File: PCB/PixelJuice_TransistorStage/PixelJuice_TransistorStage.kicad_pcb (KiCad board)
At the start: 2 copper layers, 33.2 x 35.3 mm, 12 parts, among them J1 INPUT_PORT, J2 OUTPUT_PORT, Q1 2N3904, Q2 2N3904, Q3 2N3904

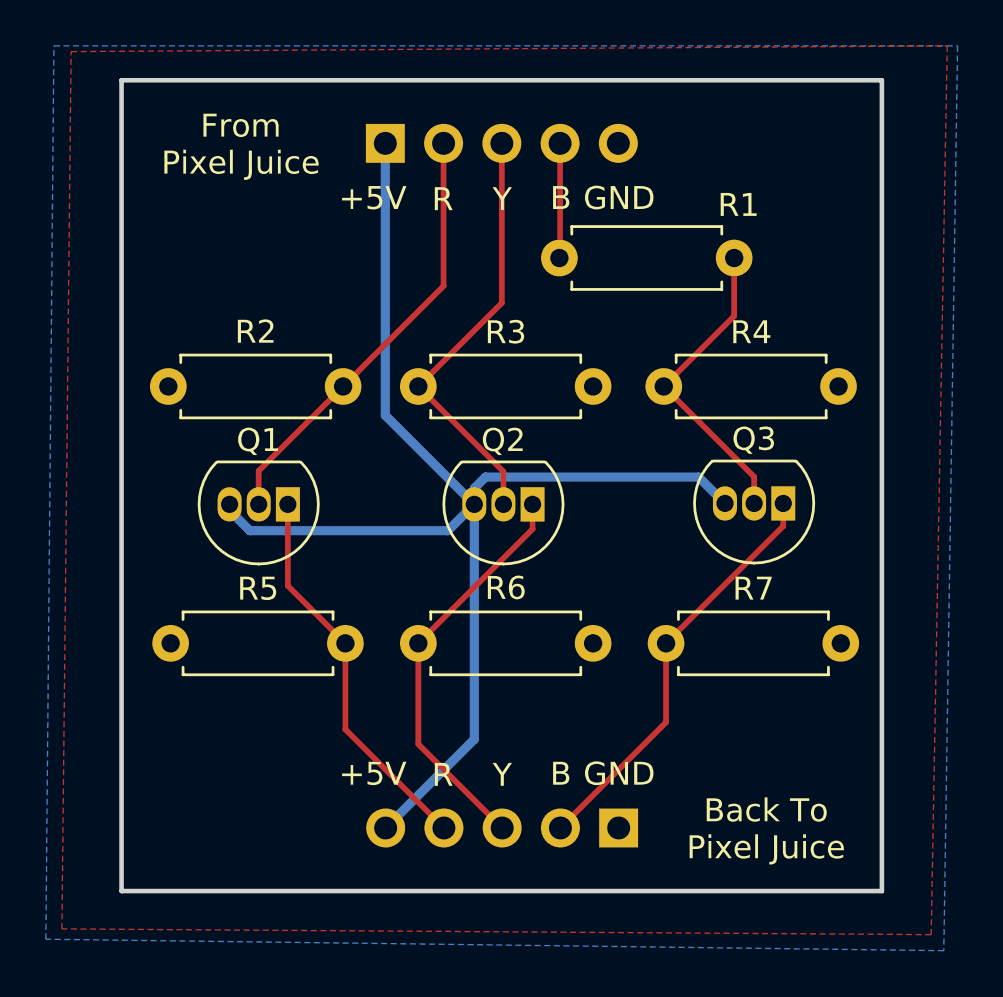
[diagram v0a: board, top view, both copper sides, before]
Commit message: added 2 new soundcard designs
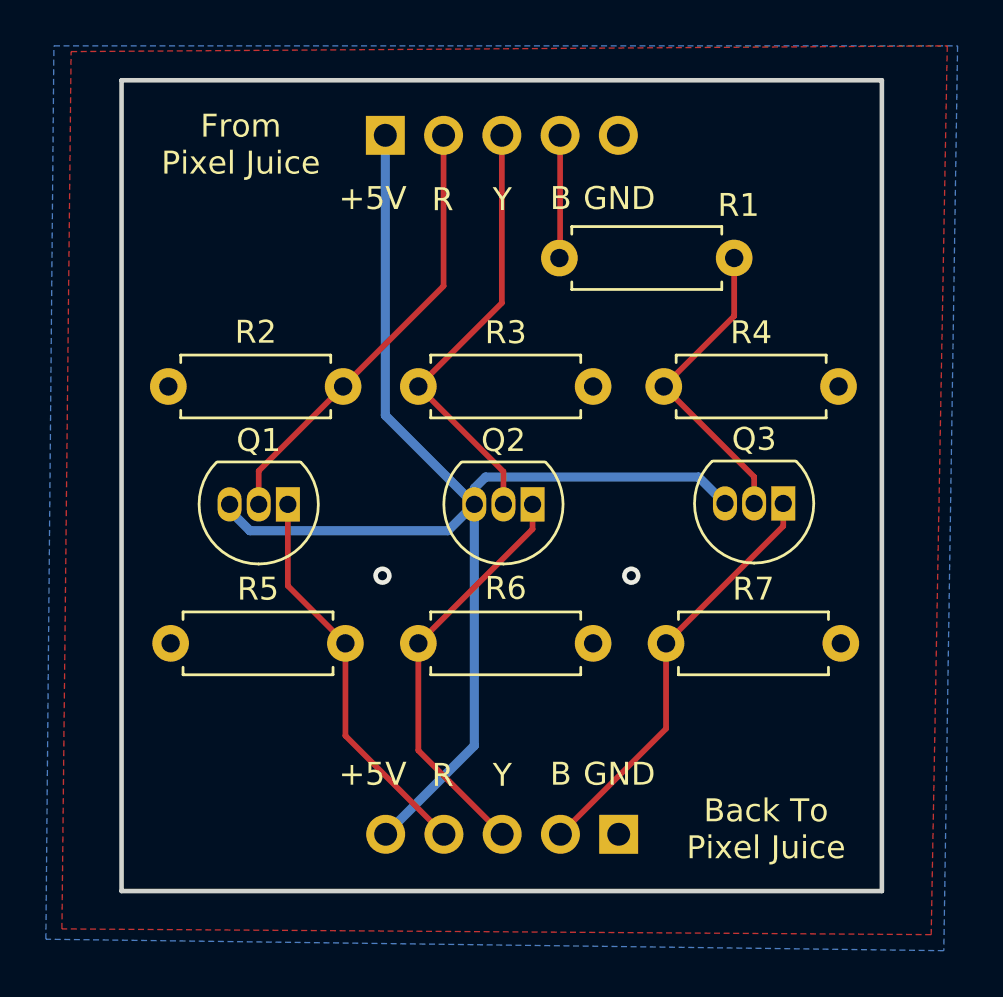
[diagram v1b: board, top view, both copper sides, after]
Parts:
- moved J1 0.35 mm to (142.2, 73.8)
- moved J2 0.28 mm to (152.3, 104.3)
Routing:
- net +5V: track 57.1 -> 57.8 mm
- net GND: vias 0 -> 2
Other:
- board text added: "JLCJLCJLCJLC"
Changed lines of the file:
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@@
       (outputformat 1)
       (mirror false)
-      (drillshape 1)
+      (drillshape 0)
       (scaleselection 1)
-      (outputdirectory "")
+      (outputdirectory "gerbers/")
     )
   )
@@
   )
   (footprint "Connector_PinHeader_2.54mm:PinHeader_1x05_P2.54mm_Vertical" (layer "B.Cu")
-    (at 152.325 104.05 90)
+    (at 152.325 104.325 90)
     (descr "Through hole straight pin header, 1x05, 2.54mm pitch, single row")
     (tags "Through hole pin header THT 1x05 2.54mm single row")
@@
     (property "Sheetname" "")
     (attr through_hole)
-    (fp_text reference "J2" (at 0 2.33 90) (layer "B.SilkS")
+    (fp_text reference "J2" (at 0 -12.575 90) (layer "B.SilkS")
       (effects (font (size 1 1) (thickness 0.15)) (justify mirror))
     )
@@
   )
   (footprint "Connector_PinHeader_2.54mm:PinHeader_1x05_P2.54mm_Vertical" (layer "B.Cu")
-    (at 142.15 74.2 -90)
+    (at 142.15 73.85 -90)
     (descr "Through hole straight pin header, 1x05, 2.54mm pitch, single row")
     (tags "Through hole pin header THT 1x05 2.54mm single row")
@@
   )
   (gr_rect (start 130.65 71.45) (end 163.8 106.8) (layer "Edge.Cuts") (width 0.2) (fill none))
+  (gr_text "JLCJLCJLCJLC" (at 147.325 99.725) (layer "B.SilkS")
+    (effects (font (size 1 1) (thickness 0.2)) (justify mirror))
+  )
   (gr_text "Transistor Stage v1\nfor Pixel Juice\nNate Rivard, 2023" (at 147 79.25) (layer "B.SilkS")
     (effects (font (size 1 1) (thickness 0.15)) (justify left mirror))
@@
   )
   (dimension (type aligned) (layer "Cmts.User")
-    (pts (xy 152.325 104.05) (xy 152.325 74.2))
-    (height 15.8)
-    (gr_text "29.8500 mm" (at 166.975 89.125 90) (layer "Cmts.User")
-      (effects (font (size 1 1) (thickness 0.15)))
-    )
-    (format (units 3) (units_format 1) (precision 4))
-    (style (thickness 0.15) (arrow_length 1.27) (text_position_mode 0) (extension_height 0.58642) (extension_offset 0.5) keep_text_aligned)
-  )
-  (dimension (type aligned) (layer "Cmts.User")
     (pts (xy 132.7 71.45) (xy 132.7 106.8))
     (height 6.449999)
@@
   )
   (dimension (type aligned) (layer "Cmts.User")
-    (pts (xy 142.125 74.2) (xy 142.125 71.45))
+    (pts (xy 142.15 73.85) (xy 142.15 71.45))
     (height -5.025)
-    (gr_text "2.7500 mm" (at 135.95 72.825 90) (layer "Cmts.User")
-      (effects (font (size 1 1) (thickness 0.15)))
-    )
-    (format (units 3) (units_format 1) (precision 4))
-    (style (thickness 0.15) (arrow_length 1.27) (text_position_mode 0) (extension_height 0.58642) (extension_offset 0.5) keep_text_aligned)
-  )
-  (dimension (type aligned) (layer "Cmts.User")
-    (pts (xy 152.325 104.05) (xy 152.325 106.8))
-    (height -5.625)
-    (gr_text "2.7500 mm" (at 156.8 105.425 90) (layer "Cmts.User")
+    (gr_text "2.4000 mm" (at 135.975 72.65 90) (layer "Cmts.User")
       (effects (font (size 1 1) (thickness 0.15)))
     )
@@
     (style (thickness 0.15) (arrow_length 1.27) (text_position_mode 0) (extension_height 0.58642) (extension_offset 0.5) keep_text_aligned)
   )
-  (segment (start 146.03 100.185) (end 142.165 104.05) (width 0.4) (layer "B.Cu") (net 1))
+  (dimension (type aligned) (layer "Cmts.User")
+    (pts (xy 152.325 104.325) (xy 152.325 106.8))
+    (height -16.525)
+    (gr_text "2.4750 mm" (at 167.7 105.5625 90) (layer "Cmts.User")
+      (effects (font (size 1 1) (thickness 0.15)))
+    )
+    (format (units 3) (units_format 1) (precision 4))
+    (style (thickness 0.15) (arrow_length 1.27) (text_position_mode 0) (extension_height 0.58642) (extension_offset 0.5) keep_text_aligned)
+  )
+  (dimension (type aligned) (layer "Cmts.User")
+    (pts (xy 152.25 104.325) (xy 152.275 73.85))
+    (height 20.954074)
+    (gr_text "30.4750 mm" (at 172.066567 89.103747 89.95299773) (layer "Cmts.User")
+      (effects (font (size 1 1) (thickness 0.15)))
+    )
+    (format (units 3) (units_format 1) (precision 4))
+    (style (thickness 0.15) (arrow_length 1.27) (text_position_mode 0) (extension_height 0.58642) (extension_offset 0.5) keep_text_aligned)
+  )
+  (segment (start 142.15 73.85) (end 142.15 86.06) (width 0.4) (layer "B.Cu") (net 1))
   (segment (start 136.247052 91.08952) (end 135.36 90.202468) (width 0.4) (layer "B.Cu") (net 1))
   (segment (start 146.03 89.24) (end 146.52 88.75) (width 0.4) (layer "B.Cu") (net 1))
-  (segment (start 142.15 86.06) (end 146.03 89.94) (width 0.4) (layer "B.Cu") (net 1))
   (segment (start 135.36 90.202468) (end 135.36 89.94) (width 0.4) (layer "B.Cu") (net 1))
   (segment (start 155.81 88.75) (end 156.96 89.9) (width 0.4) (layer "B.Cu") (net 1))
-  (segment (start 146.03 89.94) (end 146.03 100.185) (width 0.4) (layer "B.Cu") (net 1))
-  (segment (start 142.15 74.2) (end 142.15 86.06) (width 0.4) (layer "B.Cu") (net 1))
+  (segment (start 142.15 86.06) (end 146.03 89.94) (width 0.4) (layer "B.Cu") (net 1))
   (segment (start 144.88048 91.08952) (end 136.247052 91.08952) (width 0.4) (layer "B.Cu") (net 1))
   (segment (start 146.52 88.75) (end 155.81 88.75) (width 0.4) (layer "B.Cu") (net 1))
+  (segment (start 146.03 89.94) (end 146.03 100.46) (width 0.4) (layer "B.Cu") (net 1))
+  (segment (start 146.03 100.46) (end 142.165 104.325) (width 0.4) (layer "B.Cu") (net 1))
   (segment (start 146.03 89.94) (end 146.03 89.24) (width 0.4) (layer "B.Cu") (net 1))
   (segment (start 146.03 89.94) (end 144.88048 91.08952) (width 0.4) (layer "B.Cu") (net 1))
   (segment (start 140.31 84.8) (end 136.63 88.48) (width 0.25) (layer "F.Cu") (net 2))
+  (segment (start 136.63 88.48) (end 136.63 89.94) (width 0.25) (layer "F.Cu") (net 2))
+  (segment (start 144.69 73.85) (end 144.69 80.42) (width 0.25) (layer "F.Cu") (net 2))
   (segment (start 144.69 80.42) (end 140.31 84.8) (width 0.25) (layer "F.Cu") (net 2))
-  (segment (start 136.63 88.48) (end 136.63 89.94) (width 0.25) (layer "F.Cu") (net 2))
-  (segment (start 144.69 74.2) (end 144.69 80.42) (width 0.25) (layer "F.Cu") (net 2))
-  (segment (start 147.23 74.2) (end 147.23 81.16) (width 0.25) (layer "F.Cu") (net 3))
+  (segment (start 147.23 73.85) (end 147.23 81.16) (width 0.25) (layer "F.Cu") (net 3))
   (segment (start 143.59 84.8) (end 147.3 88.51) (width 0.25) (layer "F.Cu") (net 3))
   (segment (start 147.3 88.51) (end 147.3 89.94) (width 0.25) (layer "F.Cu") (net 3))
   (segment (start 147.23 81.16) (end 143.59 84.8) (width 0.25) (layer "F.Cu") (net 3))
+  (segment (start 149.77 73.85) (end 149.77 79.17) (width 0.25) (layer "F.Cu") (net 4))
   (segment (start 149.77 79.17) (end 149.74 79.2) (width 0.25) (layer "F.Cu") (net 4))
-  (segment (start 149.77 74.2) (end 149.77 79.17) (width 0.25) (layer "F.Cu") (net 4))
+  (via (at 152.875 93.05) (size 0.8) (drill 0.4) (layers "F.Cu" "B.Cu") (free) (net 5))
+  (via (at 142.025 93.05) (size 0.8) (drill 0.4) (layers "F.Cu" "B.Cu") (free) (net 5))
   (segment (start 137.9 93.49) (end 140.41 96) (width 0.25) (layer "F.Cu") (net 6))
   (segment (start 137.9 89.94) (end 137.9 93.49) (width 0.25) (layer "F.Cu") (net 6))
-  (segment (start 140.41 99.755) (end 144.705 104.05) (width 0.25) (layer "F.Cu") (net 6))
-  (segment (start 140.41 96) (end 140.41 99.755) (width 0.25) (layer "F.Cu") (net 6))
-  (segment (start 143.59 96) (end 143.59 100.395) (width 0.25) (layer "F.Cu") (net 7))
+  (segment (start 140.41 96) (end 140.41 100.03) (width 0.25) (layer "F.Cu") (net 6))
+  (segment (start 140.41 100.03) (end 144.705 104.325) (width 0.25) (layer "F.Cu") (net 6))
+  (segment (start 143.59 100.67) (end 147.245 104.325) (width 0.25) (layer "F.Cu") (net 7))
   (segment (start 148.57 91.02) (end 143.59 96) (width 0.25) (layer "F.Cu") (net 7))
-  (segment (start 143.59 100.395) (end 147.245 104.05) (width 0.25) (layer "F.Cu") (net 7))
+  (segment (start 143.59 96) (end 143.59 100.67) (width 0.25) (layer "F.Cu") (net 7))
   (segment (start 148.57 89.94) (end 148.57 91.02) (width 0.25) (layer "F.Cu") (net 7))
-  (segment (start 154.39 96) (end 154.39 99.445) (width 0.25) (layer "F.Cu") (net 8))
-  (segment (start 154.39 99.445) (end 149.785 104.05) (width 0.25) (layer "F.Cu") (net 8))
+  (segment (start 154.39 96) (end 154.39 99.72) (width 0.25) (layer "F.Cu") (net 8))
   (segment (start 159.5 89.9) (end 159.5 90.89) (width 0.25) (layer "F.Cu") (net 8))
   (segment (start 159.5 90.89) (end 154.39 96) (width 0.25) (layer "F.Cu") (net 8))
+  (segment (start 154.39 99.72) (end 149.785 104.325) (width 0.25) (layer "F.Cu") (net 8))
   (segment (start 157.36 81.73) (end 154.29 84.8) (width 0.25) (layer "F.Cu") (net 9))
   (segment (start 154.29 84.8) (end 158.23 88.74) (width 0.25) (layer "F.Cu") (net 9))
